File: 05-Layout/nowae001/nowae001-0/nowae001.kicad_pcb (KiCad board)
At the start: 2 copper layers, 25 x 16 mm, 26 parts, among them P1 USB_A_90, P2 CONN_2X1, P3 CONN_2X1, Q1 IRLML6402, U1 FT230XQ, U2 TPS62152

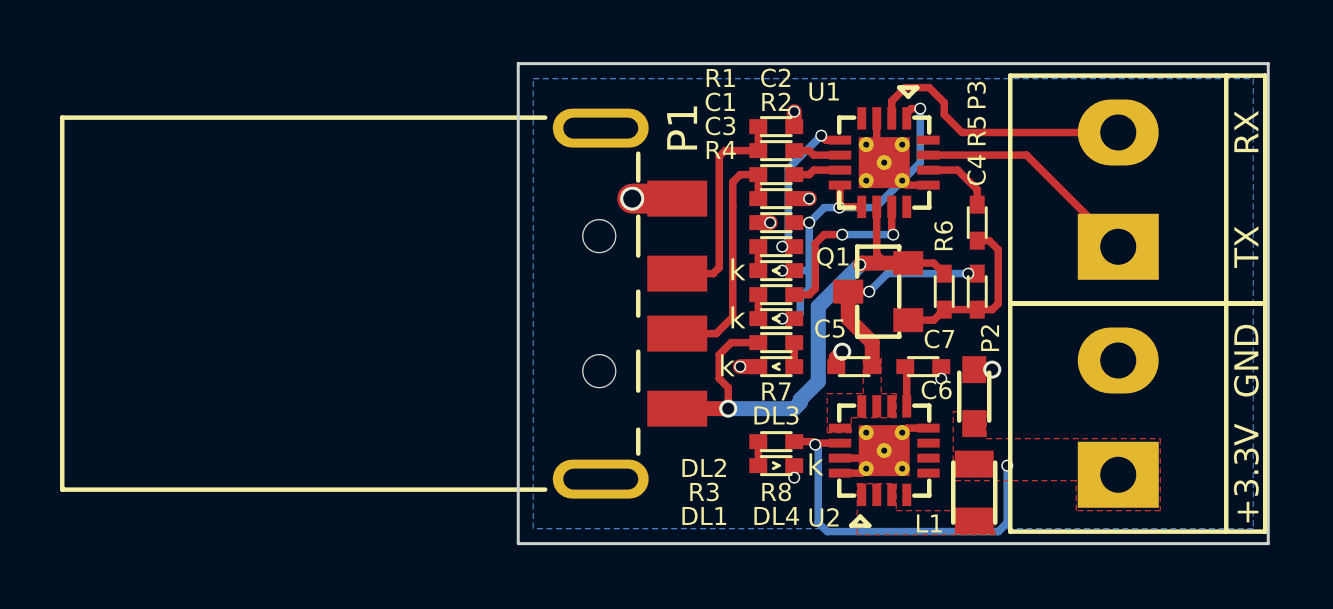
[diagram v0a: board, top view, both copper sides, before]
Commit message: Changed output connector in nowae001
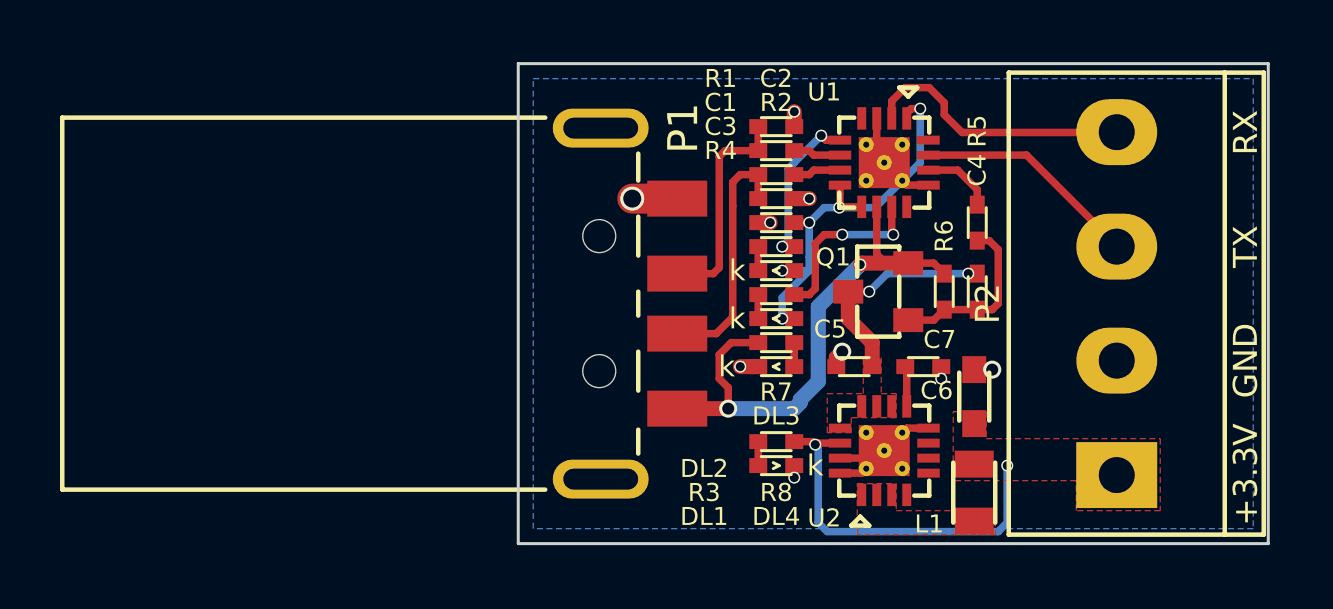
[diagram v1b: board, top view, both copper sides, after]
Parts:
- removed P3: CONN_2X1, CONNECTOR_MKDS:CONN-MKDS1_2-3.81
- P2: value CONN_2X1 -> CONN_4X1; footprint CONNECTOR_MKDS:CONN-MKDS1_2-3.81 -> CONNECTOR_MKDS:CONN-MKDS1_4-3.81
- moved P2 3.80 mm to (217.4, 135.5)

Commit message: Updated pcb in nowae001
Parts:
- DL1: value YELLOW -> GREEN
- DL2: value GREEN -> YELLOW
- U1: footprint QFN:QFN16_3x3_0.5_16+1 -> QFN:QFN16_4x4_0.65_16+1
- moved C4 8.71 mm to (207.3, 141.9), turned to 90 degrees
- moved DL2 8.25 mm to (211.6, 128.3)
- moved R6 7.97 mm to (205.0, 139.5), turned to 0 degrees
- moved Q1 7.80 mm to (205.0, 141.5), turned to 180 degrees
- moved R8 6.54 mm to (212.1, 142.7)
- moved R4 6.38 mm to (209.6, 128.3), turned to 0 degrees
- moved DL3 6.14 mm to (202.3, 142.5)
- moved DL1 5.59 mm to (211.6, 135.3)
- moved R1 5.42 mm to (204.9, 136.5)
- moved C1 5.37 mm to (204.9, 137.2)
- moved R7 5.30 mm to (202.9, 141.1), turned to 90 degrees
- moved DL4 4.34 mm to (210.0, 142.7), turned to 180 degrees
- moved C2 4.31 mm to (204.9, 133.8)
- moved R2 4.26 mm to (204.9, 134.5)
- moved C6 4.24 mm to (209.7, 141.6), turned to 180 degrees
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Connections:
- net Net-(R3-Pad2) renamed /RX_LED
- net Net-(R4-Pad1) renamed /TX_LED
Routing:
- net +3.3V: track 12.7 -> 2.10 mm, vias 2 -> 0
- net +5V: track 18.7 -> 9.23 mm, vias 2 -> 0
- net Net-(R1-Pad2): track 1.59 -> 8.21 mm
- net Net-(C1-Pad1): track 8.33 -> 2.30 mm
- net Net-(R2-Pad1): track 1.59 -> 7.55 mm
- net Net-(C2-Pad1): track 7.37 -> 2.30 mm
- net GND: track 14.0 -> 18.8 mm
- net Net-(C4-Pad2): track 5.85 -> 9.80 mm
- net /TX_LED: track 5.33 -> 1.50 mm, vias 2 -> 0
- net /RX_LED: track 5.95 -> 2.16 mm, vias 2 -> 0
- net /RX: track 9.17 -> 6.04 mm
- net /VCCIO: track 14.6 -> 11.6 mm, vias 5 -> 3
- net /EN_PWR: track 2.39 -> 5.11 mm
- net /TX: track 7.39 -> 5.98 mm
- net Net-(C4-Pad1): track 7.38 -> 7.17 mm, vias 2 -> 0
- added copper zone on F.Cu, net +5V
- added copper zone on F.Cu, net /VCCIO
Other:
- net class Default: via_dia 0.4 -> 0.7

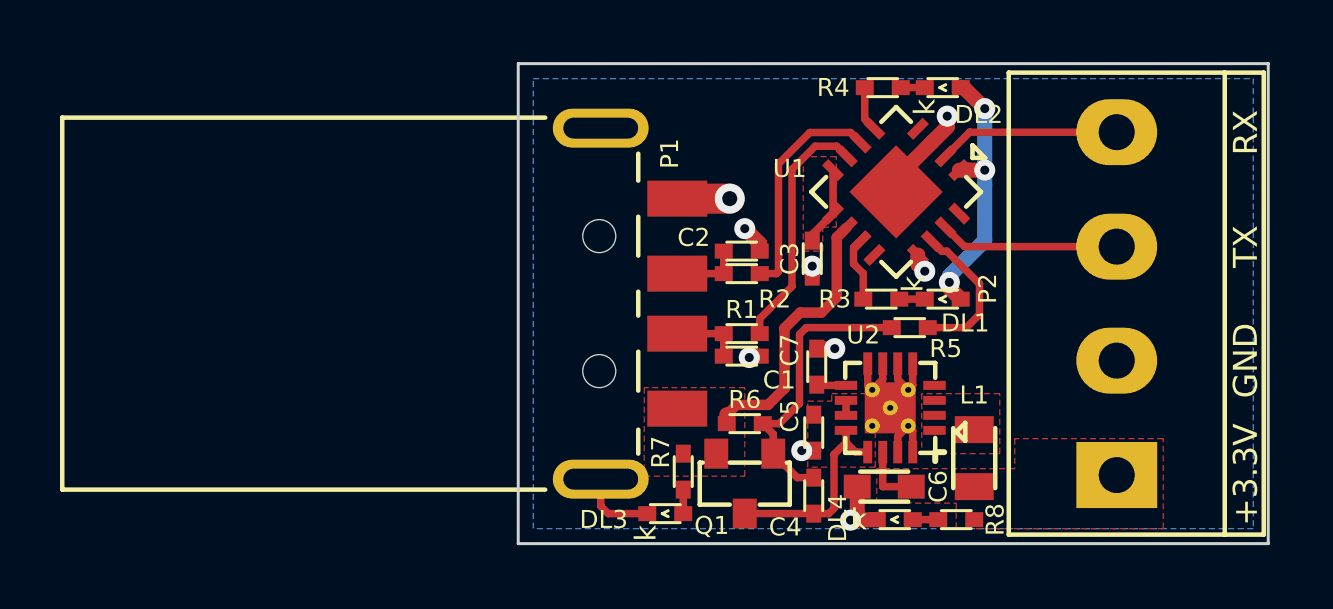
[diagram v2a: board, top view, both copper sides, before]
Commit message: Added logos in nowae001
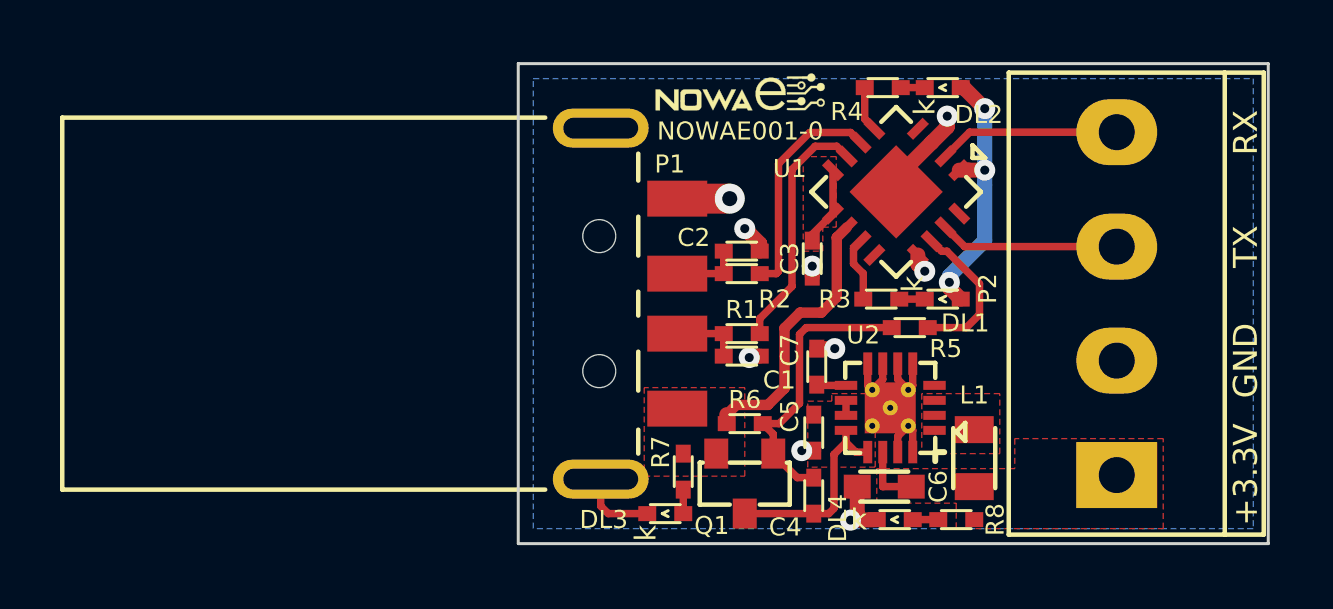
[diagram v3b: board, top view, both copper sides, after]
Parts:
- added G***: LOGO, LOGO:Untitled, F.Cu at (204.8, 128.3)
- added G***: LOGO, LOGO:Logo_silk_CC-BY-SA_5x2mm, B.Cu at (204.4, 129.9)
- added G***: LOGO, LOGO:Logo_silk_OSHW_6x6mm, B.Cu at (209.7, 129.9)
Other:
- board text added: "NOWAE001-0"
